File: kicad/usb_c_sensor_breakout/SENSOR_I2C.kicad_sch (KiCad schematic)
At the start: 5 parts, among them J2 Conn_01x06

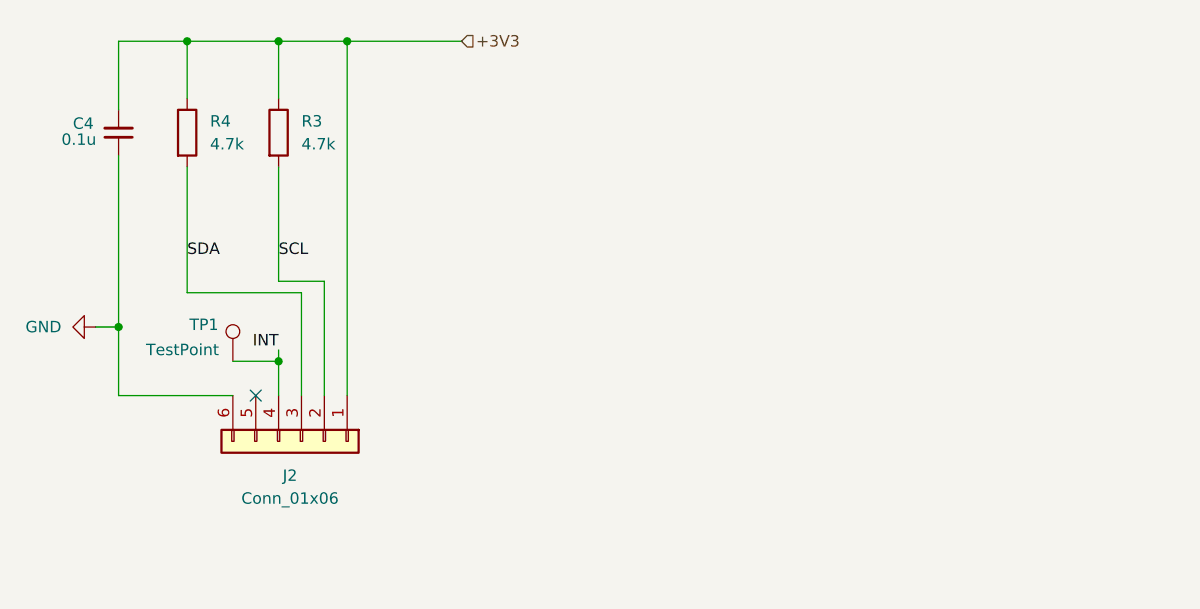
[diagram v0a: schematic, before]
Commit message: Commit3: Regulators + Top-level + I2C sensor upgrade
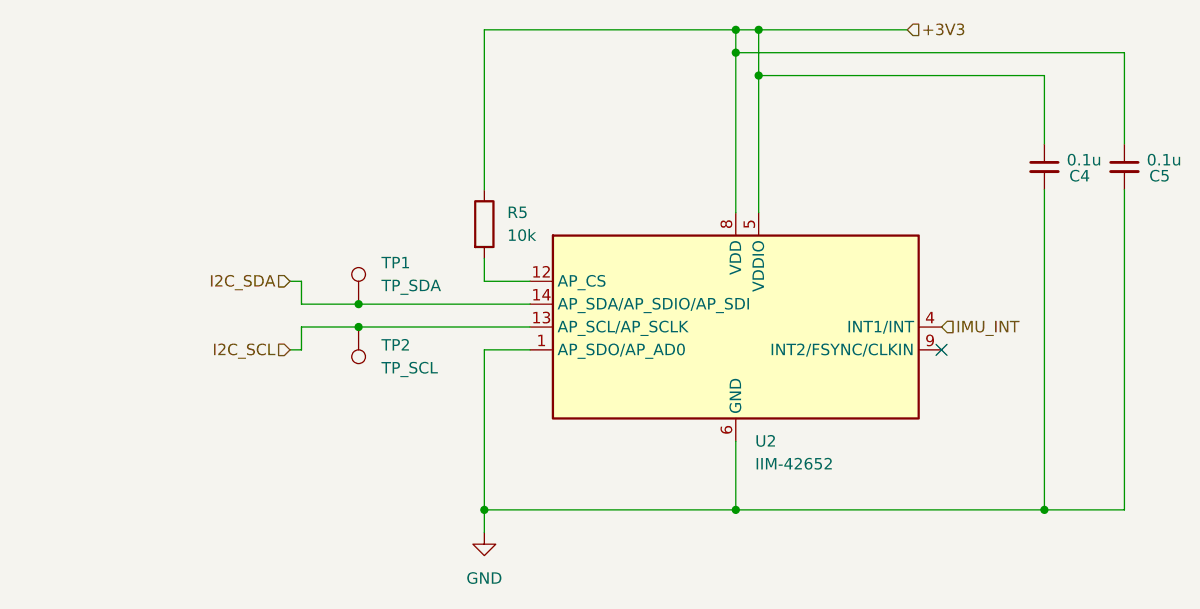
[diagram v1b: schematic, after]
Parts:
- removed J2: Conn_01x06, symbol Connector_Generic:Conn_01x06
- removed R3, R4: 4.7k, symbol Device:R
- added C5: 0.1u, symbol Device:C_Small
- added R5: 10k, symbol Device:R
- added TP2: TP_SCL, symbol Connector:TestPoint
- added U2: IIM-42652, Package_LGA:Bosch_LGA-14_3x2.5mm_P0.5mm, symbol Sensor_Motion:IIM-42652
- TP1: value TestPoint -> TP_SDA
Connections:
- net +3V3: now also C4.1, C5.1, R5.1, U2.5 (VDDIO), U2.8 (VDD); no longer C4.2
- net GND: now also C4.2, C5.2, U2.1 (AP_SDO/AP_AD0), U2.6 (GND), U2.7 (GND); no longer C4.1
- net INT renamed I2C_SDA
- net I2C_SDA: now also U2.14 (AP_SDA/AP_SDIO/AP_SDI)
- new net: R5.2, U2.12 (AP_CS)
- new net I2C_SCL: TP2.1, U2.13 (AP_SCL/AP_SCLK)
- new net IMU_INT: U2.4 (INT1/INT)
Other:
- moved on the sheet: C4

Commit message: Commit 4: Updated annotation + footprints
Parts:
- C4, C5: footprint (none) -> Capacitor_SMD:C_0603_1608Metric
- R5: footprint (none) -> Resistor_SMD:R_0603_1608Metric
- TP1, TP2: footprint (none) -> TestPoint:TestPoint_Pad_D1.5mm
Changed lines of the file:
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@@
 			)
 		)
-		(property "Footprint" ""
+		(property "Footprint" "TestPoint:TestPoint_Pad_D1.5mm"
 			(at 107.95 91.44 0)
 			(effects
@@
 			)
 		)
-		(property "Footprint" ""
+		(property "Footprint" "Capacitor_SMD:C_0603_1608Metric"
 			(at 189.23 73.66 0)
 			(effects
@@
 			)
 		)
-		(property "Footprint" ""
+		(property "Footprint" "Resistor_SMD:R_0603_1608Metric"
 			(at 125.222 80.01 90)
 			(effects
@@
 			)
 		)
-		(property "Footprint" ""
+		(property "Footprint" "TestPoint:TestPoint_Pad_D1.5mm"
 			(at 118.11 88.9 0)
 			(effects
@@
 			)
 		)
-		(property "Footprint" ""
+		(property "Footprint" "Capacitor_SMD:C_0603_1608Metric"
 			(at 198.12 73.66 0)
 			(effects

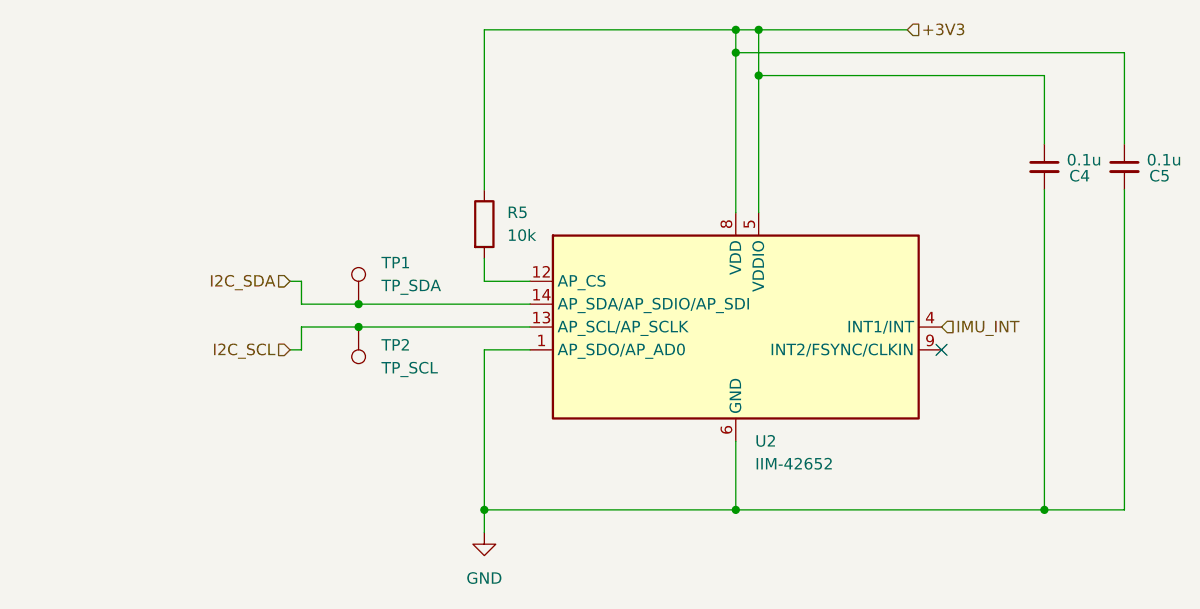
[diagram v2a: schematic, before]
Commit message: Commit 5: MCU + Final Schematic Touches + Labelling + USBc fix
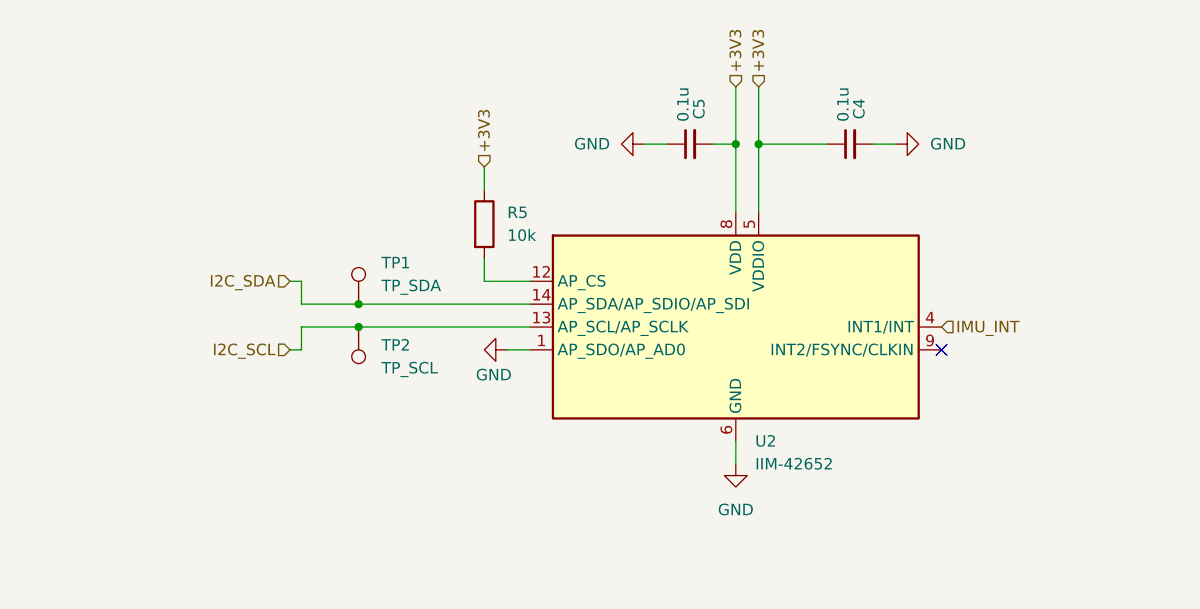
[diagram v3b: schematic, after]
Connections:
- net +3V3: now also C5.2; no longer C5.1
- net GND: now also C5.1; no longer C5.2
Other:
- moved on the sheet: C4, C5

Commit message: Commit 6: Finished PCB + Updated Schematic
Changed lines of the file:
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@@
 	)
 	(hierarchical_label "I2C_SDA"
-		(shape input)
+		(shape bidirectional)
 		(at 105.41 86.36 180)
 		(effects
@@
 	)
 	(hierarchical_label "IMU_INT"
-		(shape input)
+		(shape output)
 		(at 177.8 91.44 0)
 		(effects
